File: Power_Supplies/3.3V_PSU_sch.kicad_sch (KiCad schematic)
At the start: 10 parts, among them U1 TPS62822DLC

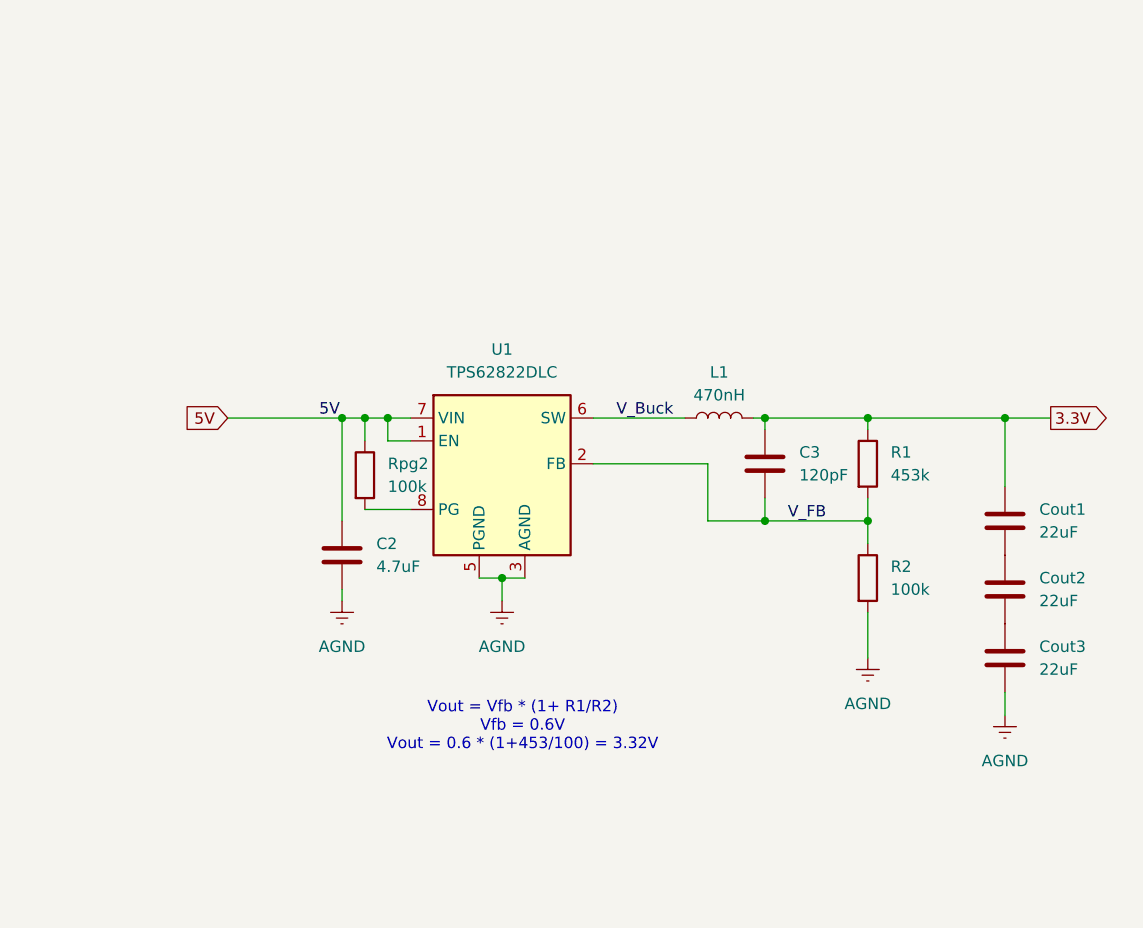
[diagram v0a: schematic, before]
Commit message: Updated power supplies and added DAC circuitry
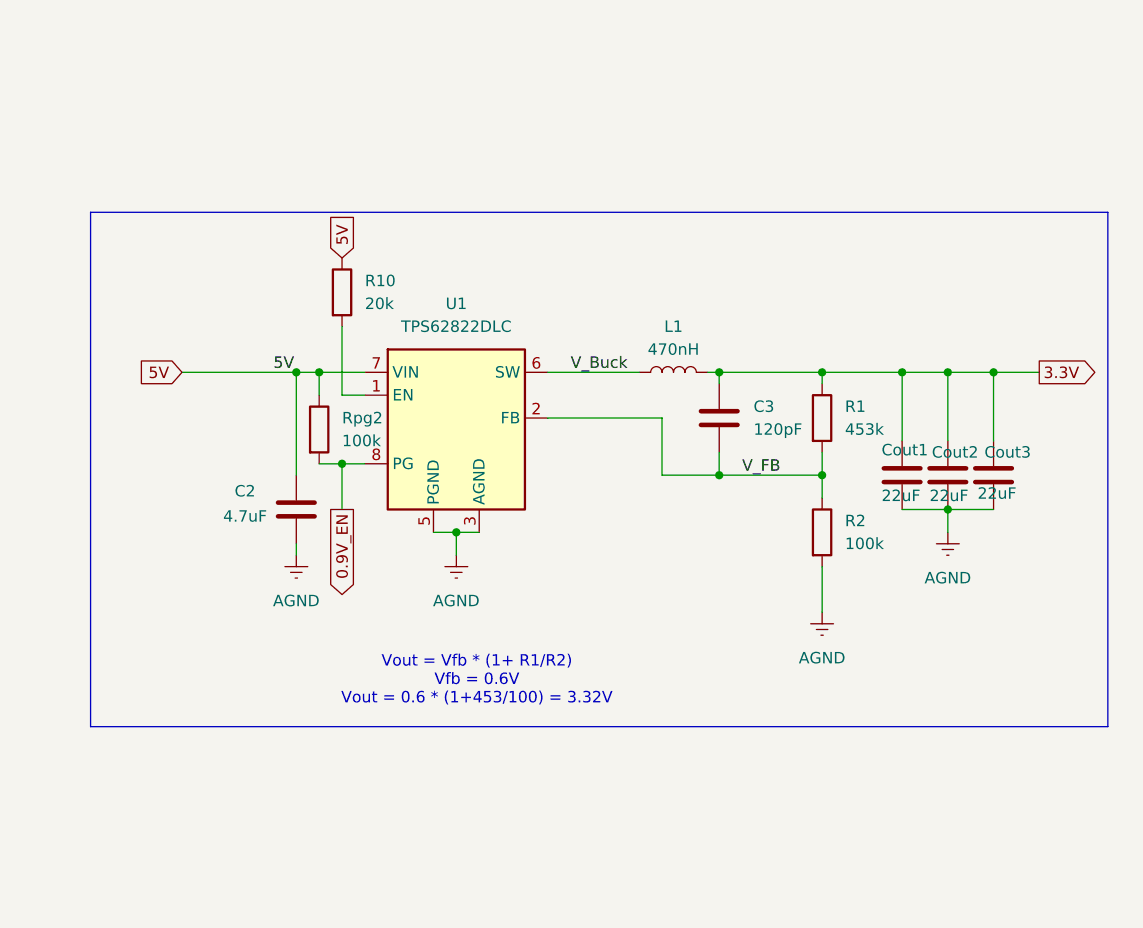
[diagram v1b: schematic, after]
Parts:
- added R10: 20k, Resistor_SMD:R_0805_2012Metric, symbol Device:R
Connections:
- net 3.3V: now also Cout2.1, Cout3.1
- net 5V: now also R10.1; no longer U1.1 (EN)
- net AGND: now also Cout1.2, Cout2.2
- net 0.9V_EN: now reaches Rpg2.2, U1.8 (PG)
- new net: R10.2, U1.1 (EN)
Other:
- moved on the sheet: C2, C3, Cout1, L1, R1, R2, Rpg2, U1

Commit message: Finished HiZ Inputs
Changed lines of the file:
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@@
 	)
 	(rectangle
-		(start 96.52 63.5)
+		(start 96.52 60.96)
 		(end 209.55 120.65)
 		(stroke

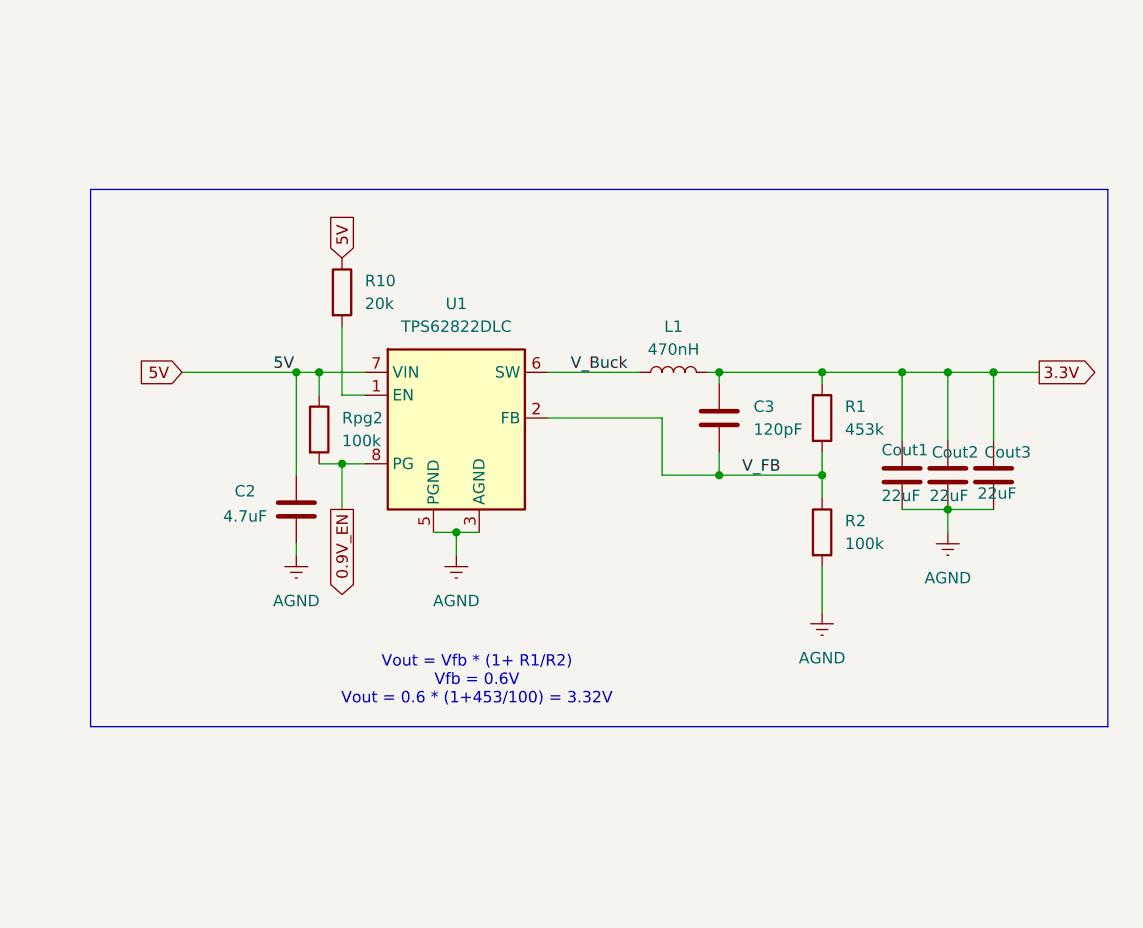
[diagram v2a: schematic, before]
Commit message: Added 3.3V/1.8V LDO, clock IC
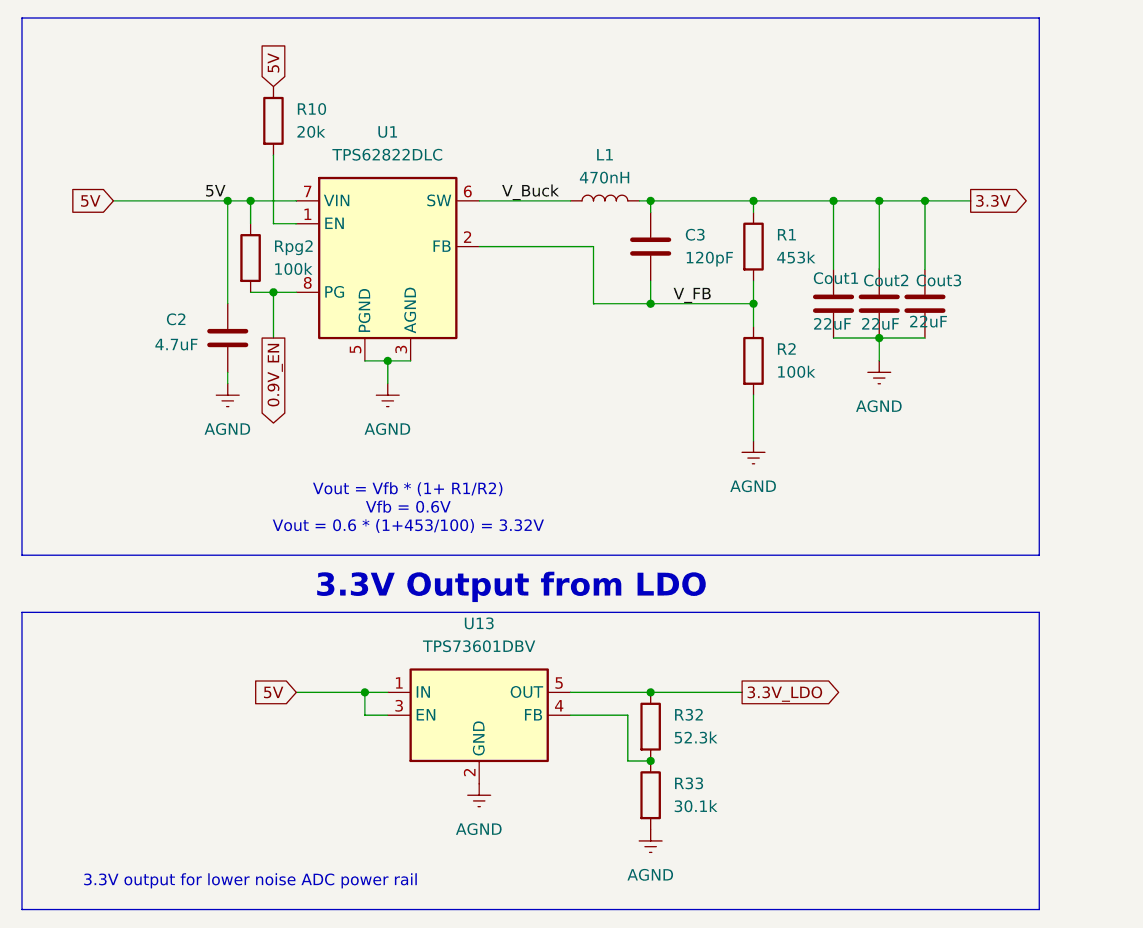
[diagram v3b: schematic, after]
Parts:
- added R32: 52.3k, Resistor_SMD:R_0805_2012Metric, symbol Device:R
- added R33: 30.1k, Resistor_SMD:R_0805_2012Metric, symbol Device:R
- added U13: TPS73601DBV, Package_TO_SOT_SMD:SOT-23-5, symbol Regulator_Linear:TPS73601DBV
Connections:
- net 5V: now also U13.1 (IN), U13.3 (EN)
- net AGND: now also R33.2, U13.2 (GND)
- new net: R32.2, R33.1, U13.4 (FB)
- new net 3.3V_LDO: R32.1, U13.5 (OUT)
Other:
- note added: "3.3V Output from LDO"
- note added: "3.3V output for lower noise ADC power rail"
- moved on the sheet: C2, C3, Cout1, Cout2, Cout3, L1, R1, R10, R2, Rpg2, U1

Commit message: big things are coming...
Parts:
- renumbered C2 to C1, C3 to C2, R10 to R1, R32 to R2, R33 to R3, R1 to R4, R2 to R5, Rpg2 to Rpg1, U13 to U2

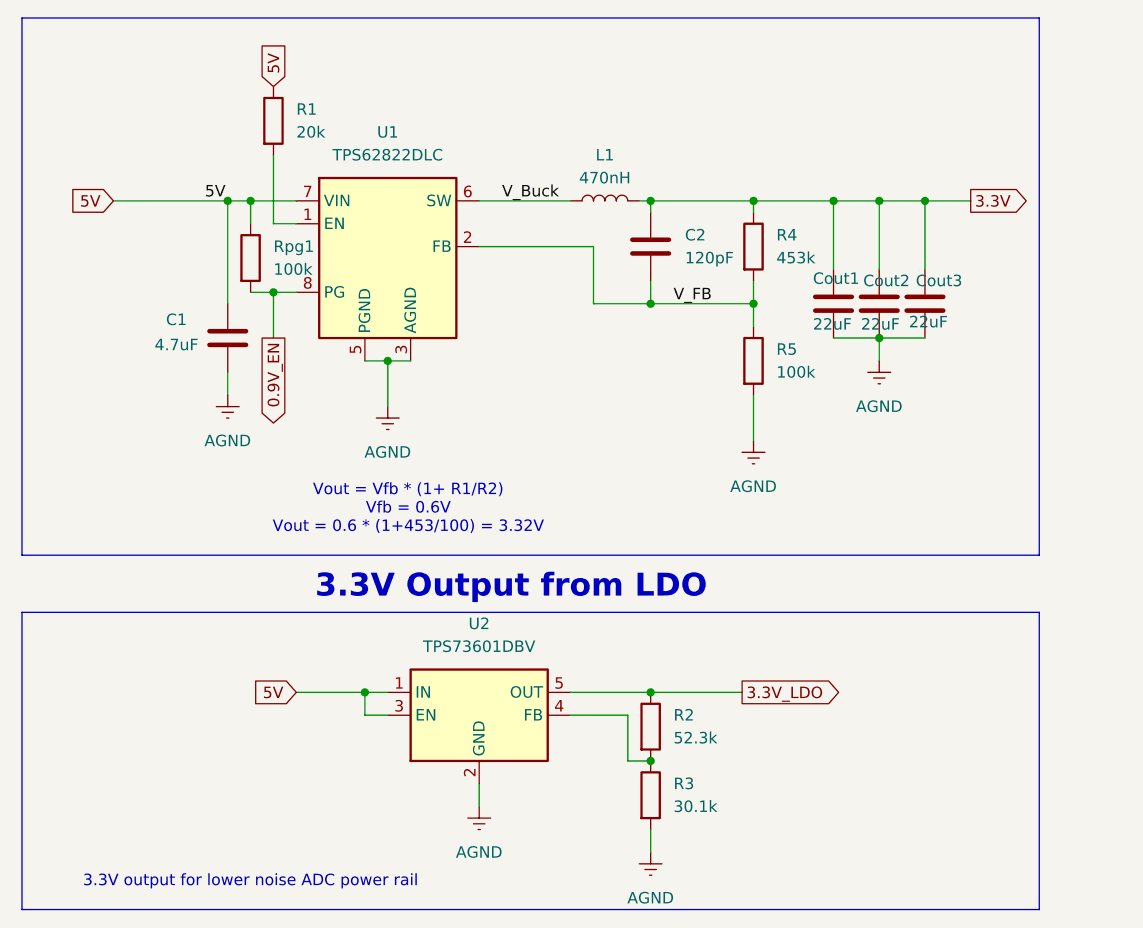
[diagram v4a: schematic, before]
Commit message: Added stuff for the power supply circuitry
changed all grounds to GND (same ground plane)
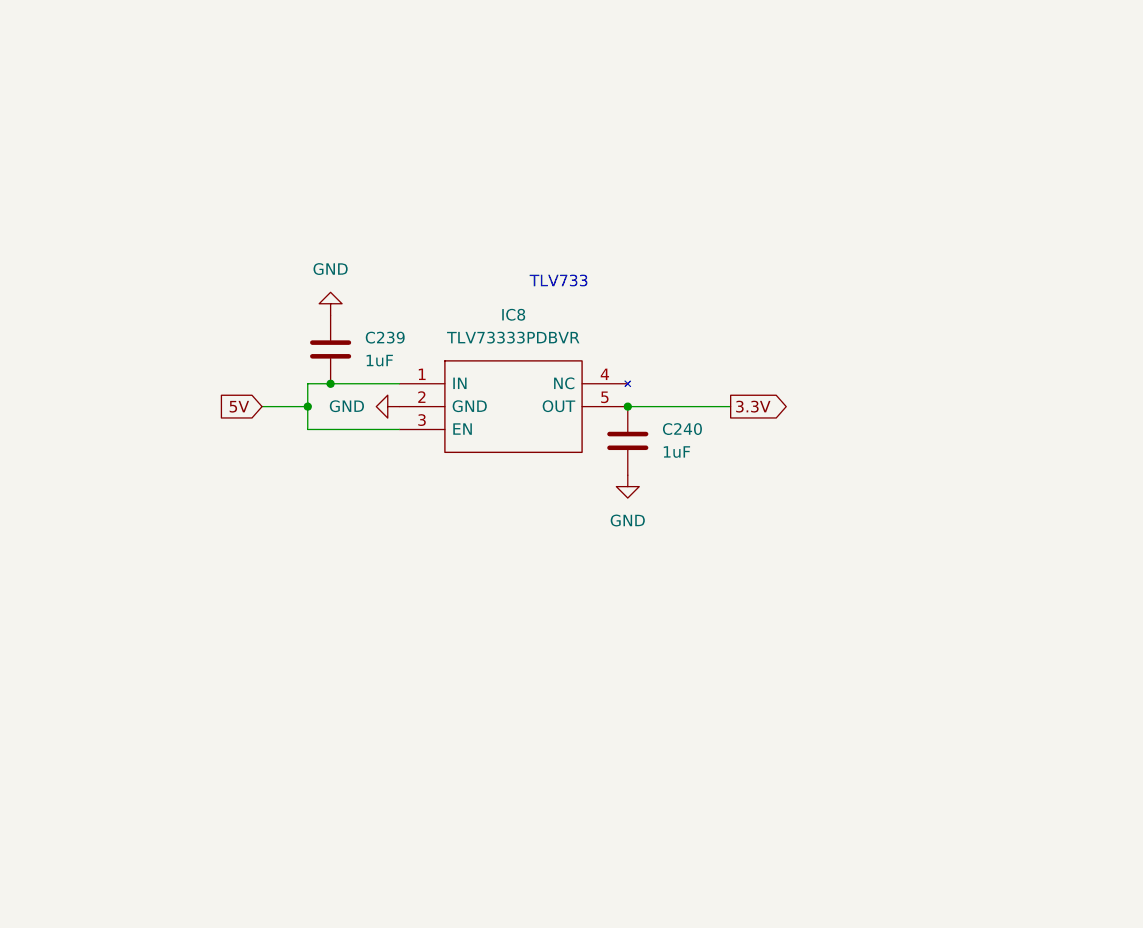
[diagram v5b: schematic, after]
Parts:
- removed C1: 4.7uF, Capacitor_SMD:C_0805_2012Metric, symbol Device:C
- removed C2: 120pF, Capacitor_SMD:C_0402_1005Metric, symbol Device:C
- removed Cout1, Cout2, Cout3: 22uF, Capacitor_SMD:C_0805_2012Metric, symbol Device:C
- removed L1: 470nH, Inductor_SMD:L_0805_2012Metric, symbol Device:L
- removed R1: 20k, Resistor_SMD:R_0805_2012Metric, symbol Device:R
- removed R2: 52.3k, Resistor_SMD:R_0805_2012Metric, symbol Device:R
- removed R3: 30.1k, Resistor_SMD:R_0805_2012Metric, symbol Device:R
- removed R4: 453k, Resistor_SMD:R_0805_2012Metric, symbol Device:R
- removed R5, Rpg1: 100k, Resistor_SMD:R_0805_2012Metric, symbol Device:R
- removed U1: TPS62822DLC, Package_SON:Texas_VSON-HR-8_1.5x2mm_P0.5mm, symbol Regulator_Switching:TPS62822DLC
- removed U2: TPS73601DBV, Package_TO_SOT_SMD:SOT-23-5, symbol Regulator_Linear:TPS73601DBV
- added C239, C240: 1uF, Capacitor_SMD:C_0402_1005Metric, symbol Device:C
- added IC8: TLV73333PDBVR, SOT95P280X145-5N, symbol SamacSys_Parts:TLV73333PDBVR
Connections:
- net 3.3V: now also C240.1, IC8.5 (OUT)
- net 5V: now also C239.2, IC8.1 (IN), IC8.3 (EN)
- new net GND: C239.1, C240.2, IC8.2 (GND)
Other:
- note added: "TLV733"
- note removed: "3.3V Output from LDO"
- note removed: "3.3V output for lower noise ADC power rail"
- note removed: "Vout = Vfb * (1+ R1/R2) Vfb = 0.6V Vout = 0.6 * (1+453/100) = 3.32V"
